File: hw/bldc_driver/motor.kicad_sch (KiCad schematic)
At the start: 103 parts, among them Q1 IRF540N, Q2 IRF540N, Q3 IRF540N, Q4 IRF540N, Q5 IRF540N, Q6 IRF540N, U10 TPS54202DDC, U11 AMC1200BDWV, U12 AMC1200BDWV, U13 AMC1200BDWV, U2 STGAP2SCM, U3 STGAP2SCM, U4 STGAP2SCM, U5 STGAP2SCM, U6 STGAP2SCM, U7 STGAP2SCM, U9 AMC1200BDWV

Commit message: feat: add CNCs
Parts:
- renumbered Rshunt to Rshunt1
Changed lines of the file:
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@@
 (kicad_sch
-	(version 20231120)
+	(version 20250114)
 	(generator "eeschema")
-	(generator_version "8.0")
+	(generator_version "9.0")
 	(paper "A4")
+	(rectangle
+		(start 124.46 13.335)
+		(end 147.955 165.1)
+		(stroke
+			(width -0.0001)
+			(type default)
+		)
+		(fill
+			(type color)
+			(color 0 132 0 0.3)
+		)
+	)
+	(rectangle
+		(start 139.7 13.335)
+		(end 167.64 94.615)
+		(stroke
+			(width -0.0001)
+			(type default)
+		)
+		(fill
+			(type color)
+			(color 0 132 0 0.3)
+		)
+	)
+	(rectangle
+		(start 167.64 13.335)
+		(end 254 94.615)
+		(stroke
+			(width -0.0001)
+			(type default)
+		)
+		(fill
+			(type color)
+			(color 132 0 0 0.3)
+		)
+	)
+	(rectangle
+		(start 147.955 94.615)
+		(end 254 165.1)
+		(stroke
+			(width -0.0001)
+			(type default)
+		)
+		(fill
+			(type color)
+			(color 132 0 0 0.3)
+		)
+	)
+	(rectangle
+		(start 155.575 119.38)
+		(end 246.38 161.29)
+		(stroke
+			(width 0)
+			(type default)
+		)
+		(fill
+			(type none)
+		)
+	)
+	(rectangle
+		(start 39.37 13.335)
+		(end 124.46 165.1)
+		(stroke
+			(width -0.0001)
+			(type default)
+		)
+		(fill
+			(type color)
+			(color 132 0 0 0.3)
+		)
+	)
+	(rectangle
+		(start 254 94.615)
+		(end 283.845 165.1)
+		(stroke
+			(width -0.0001)
+			(type default)
+		)
+		(fill
+			(type color)
+			(color 0 132 0 0.3)
+		)
+	)
+	(rectangle
+		(start 12.7 13.335)
+		(end 39.37 165.1)
+		(stroke
+			(width -0.0001)
+			(type default)
+		)
+		(fill
+			(type color)
+			(color 0 132 0 0.3)
+		)
+	)
+	(rectangle
+		(start 254 13.335)
+		(end 283.845 94.615)
+		(stroke
+			(width -0.0001)
+			(type default)
+		)
+		(fill
+			(type color)
+			(color 0 132 0 0.3)
+		)
+	)
+	(text "12V POWER"
+		(exclude_from_sim no)
+		(at 103.886 18.288 0)
+		(effects
+			(font
+				(size 3.81 3.81)
+				(color 255 0 0 1)
+			)
+		)
+	)
+	(text "3.3V MCU"
+		(exclude_from_sim no)
+		(at 269.494 17.272 0)
+		(effects
+			(font
+				(size 3.81 3.81)
+				(color 0 255 0 1)
+			)
+		)
+	)
+	(text "5V ADC DCDC"
+		(exclude_from_sim no)
+		(at 176.276 116.84 0)
+		(effects
+			(font
+				(size 3.81 3.81)
+				(color 255 0 0 1)
+			)
+		)
+	)
+	(text_box "Phase W Isolated Gate Drivers"
+		(exclude_from_sim no)
+		(at 157.48 13.335 0)
+		(size 31.75 7.62)
+		(margins 0.9525 0.9525 0.9525 0.9525)
+		(stroke
+			(width 0)
+			(type default)
+		)
+		(fill
+			(type none)
+		)
+		(effects
+			(font
+				(size 1.27 1.27)
+			)
+			(justify left top)
+		)
+	)
+	(text_box "Phase V Isolated Gate Drivers"
+		(exclude_from_sim no)
+		(at 36.195 89.535 0)
+		(size 31.75 7.62)
+		(margins 0.9525 0.9525 0.9525 0.9525)
+		(stroke
+			(width 0)
+			(type default)
+		)
+		(fill
+			(type none)
+		)
+		(effects
+			(font
+				(size 1.27 1.27)
+			)
+			(justify left top)
+		)
+	)
+	(text_box "Phase U Isolated Gate Drivers"
+		(exclude_from_sim no)
+		(at 36.83 13.335 0)
+		(size 31.75 7.62)
+		(margins 0.9525 0.9525 0.9525 0.9525)
+		(stroke
+			(width 0)
+			(type default)
+		)
+		(fill
+			(type none)
+		)
+		(effects
+			(font
+				(size 1.27 1.27)
+			)
+			(justify left top)
+		)
+	)
+	(text_box "Vout = Vref * (R4/R5 + 1) = 0.596 * (200k/27k + 1) = 5.010V"
+		(exclude_from_sim no)
+		(at 210.185 151.13 0)
+		(size 34.925 8.255)
+		(margins 0.9525 0.9525 0.9525 0.9525)
+		(stroke
+			(width 0)
+			(type default)
+		)
+		(fill
+			(type none)
+		)
+		(effects
+			(font
+				(size 1.27 1.27)
+			)
+			(justify left top)
+		)
+	)
 	(junction
 		(at 76.2 142.24)
@@
 		)
 	)
-	(rectangle
-		(start 124.46 13.335)
-		(end 147.955 165.1)
-		(stroke
-			(width -0.0001)
-			(type default)
-		)
-		(fill
-			(type color)
-			(color 0 132 0 0.3)
-		)
-	)
-	(rectangle
-		(start 139.7 13.335)
-		(end 167.64 94.615)
-		(stroke
-			(width -0.0001)
-			(type default)
-		)
-		(fill
-			(type color)
-			(color 0 132 0 0.3)
-		)
-	)
-	(rectangle
-		(start 167.64 13.335)
-		(end 254 94.615)
-		(stroke
-			(width -0.0001)
-			(type default)
-		)
-		(fill
-			(type color)
-			(color 132 0 0 0.3)
-		)
-	)
-	(rectangle
-		(start 147.955 94.615)
-		(end 254 165.1)
-		(stroke
-			(width -0.0001)
-			(type default)
-		)
-		(fill
-			(type color)
-			(color 132 0 0 0.3)
-		)
-	)
-	(rectangle
-		(start 155.575 119.38)
-		(end 246.38 161.29)
-		(stroke
-			(width 0)
-			(type default)
-		)
-		(fill
-			(type none)
-		)
-	)
-	(rectangle
-		(start 39.37 13.335)
-		(end 124.46 165.1)
-		(stroke
-			(width -0.0001)
-			(type default)
-		)
-		(fill
-			(type color)
-			(color 132 0 0 0.3)
-		)
-	)
-	(rectangle
-		(start 254 94.615)
-		(end 283.845 165.1)
-		(stroke
-			(width -0.0001)
-			(type default)
-		)
-		(fill
-			(type color)
-			(color 0 132 0 0.3)
-		)
-	)
-	(rectangle
-		(start 12.7 13.335)
-		(end 39.37 165.1)
-		(stroke
-			(width -0.0001)
-			(type default)
-		)
-		(fill
-			(type color)
-			(color 0 132 0 0.3)
-		)
-	)
-	(rectangle
-		(start 254 13.335)
-		(end 283.845 94.615)
-		(stroke
-			(width -0.0001)
-			(type default)
-		)
-		(fill
-			(type color)
-			(color 0 132 0 0.3)
-		)
-	)
-	(text_box "Phase W Isolated Gate Drivers"
-		(exclude_from_sim no)
-		(at 157.48 13.335 0)
-		(size 31.75 7.62)
-		(stroke
-			(width 0)
-			(type default)
-		)
-		(fill
-			(type none)
-		)
-		(effects
-			(font
-				(size 1.27 1.27)
-			)
-			(justify left top)
-		)
-	)
-	(text_box "Phase V Isolated Gate Drivers"
-		(exclude_from_sim no)
-		(at 36.195 89.535 0)
-		(size 31.75 7.62)
-		(stroke
-			(width 0)
-			(type default)
-		)
-		(fill
-			(type none)
-		)
-		(effects
-			(font
-				(size 1.27 1.27)
-			)
-			(justify left top)
-		)
-	)
-	(text_box "Phase U Isolated Gate Drivers"
-		(exclude_from_sim no)
-		(at 36.83 13.335 0)
-		(size 31.75 7.62)
-		(stroke
-			(width 0)
-			(type default)
-		)
-		(fill
-			(type none)
-		)
-		(effects
-			(font
-				(size 1.27 1.27)
-			)
-			(justify left top)
-		)
-	)
-	(text_box "Vout = Vref * (R4/R5 + 1) = 0.596 * (200k/27k + 1) = 5.010V"
-		(exclude_from_sim no)
-		(at 210.185 151.13 0)
-		(size 34.925 8.255)
-		(stroke
-			(width 0)
-			(type default)
-		)
-		(fill
-			(type none)
-		)
-		(effects
-			(font
-				(size 1.27 1.27)
-			)
-			(justify left top)
-		)
-	)
-	(text "12V POWER"
-		(exclude_from_sim no)
-		(at 103.886 18.288 0)
-		(effects
-			(font
-				(size 3.81 3.81)
-				(color 255 0 0 1)
-			)
-		)
-	)
-	(text "3.3V MCU"
-		(exclude_from_sim no)
-		(at 269.494 17.272 0)
-		(effects
-			(font
-				(size 3.81 3.81)
-				(color 0 255 0 1)
-			)
-		)
-	)
-	(text "5V ADC DCDC"
-		(exclude_from_sim no)
-		(at 176.276 116.84 0)
-		(effects
-			(font
-				(size 3.81 3.81)
-				(color 255 0 0 1)
-			)
-		)
-	)
 	(hierarchical_label "PH_U_HI"
 		(shape input)
@@
 		(on_board yes)
 		(dnp no)
-		(property "Reference" "Rshunt"
+		(property "Reference" "Rshunt1"
 			(at 227.584 108.712 90)
 			(effects
@@
 			(project ""
 				(path "/6f0070f8-99b2-4a48-98f9-774d985c191f/19ba0eb6-9d44-4933-bb79-a8302d3dae46"
-					(reference "Rshunt")
+					(reference "Rshunt1")
 					(unit 1)
 				)

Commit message: feat: start PCB
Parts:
- C10, C12, C14, C33, C35, C37, C43, C45, C47, C49, C51, C53: footprint 0805 (2012 Metric) -> Capacitor_SMD:C_0805_2012Metric_Pad1.18x1.45mm_HandSolder
- Rshunt1: value R -> HoLLR2512-3W-15mR-1%
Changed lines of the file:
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@@
 			)
 		)
-		(property "Footprint" "0805 (2012 Metric)"
+		(property "Footprint" "Capacitor_SMD:C_0805_2012Metric_Pad1.18x1.45mm_HandSolder"
 			(at 45.4152 138.43 0)
 			(effects
@@
 			)
 		)
-		(property "Footprint" "0805 (2012 Metric)"
+		(property "Footprint" "Capacitor_SMD:C_0805_2012Metric_Pad1.18x1.45mm_HandSolder"
 			(at 152.0952 30.48 0)
 			(effects
@@
 			)
 		)
-		(property "Footprint" "0805 (2012 Metric)"
+		(property "Footprint" "Capacitor_SMD:C_0805_2012Metric_Pad1.18x1.45mm_HandSolder"
 			(at 30.1752 138.43 0)
 			(effects
@@
 			)
 		)
-		(property "Footprint" "0805 (2012 Metric)"
+		(property "Footprint" "Capacitor_SMD:C_0805_2012Metric_Pad1.18x1.45mm_HandSolder"
 			(at 174.9552 29.21 0)
 			(effects
@@
 			)
 		)
-		(property "Footprint" "0805 (2012 Metric)"
+		(property "Footprint" "Capacitor_SMD:C_0805_2012Metric_Pad1.18x1.45mm_HandSolder"
 			(at 25.0952 106.68 0)
 			(effects
@@
 			)
 		)
-		(property "Value" "R"
-			(at 229.87 106.172 90)
+		(property "Value" "HoLLR2512-3W-15mR-1%"
+			(at 225.552 118.618 90)
 			(effects
 				(font
@@
 			)
 		)
-		(property "Footprint" "0805 (2012 Metric)"
+		(property "Footprint" "Capacitor_SMD:C_0805_2012Metric_Pad1.18x1.45mm_HandSolder"
 			(at 45.4152 62.23 0)
 			(effects
@@
 			)
 		)
-		(property "Footprint" "0805 (2012 Metric)"
+		(property "Footprint" "Capacitor_SMD:C_0805_2012Metric_Pad1.18x1.45mm_HandSolder"
 			(at 46.6852 30.48 0)
 			(effects
@@
 			)
 		)
-		(property "Footprint" "0805 (2012 Metric)"
+		(property "Footprint" "Capacitor_SMD:C_0805_2012Metric_Pad1.18x1.45mm_HandSolder"
 			(at 46.6852 105.41 0)
 			(effects
@@
 			)
 		)
-		(property "Footprint" "0805 (2012 Metric)"
+		(property "Footprint" "Capacitor_SMD:C_0805_2012Metric_Pad1.18x1.45mm_HandSolder"
 			(at 173.6852 68.58 0)
 			(effects
@@
 			)
 		)
-		(property "Footprint" "0805 (2012 Metric)"
+		(property "Footprint" "Capacitor_SMD:C_0805_2012Metric_Pad1.18x1.45mm_HandSolder"
 			(at 30.1752 62.23 0)
 			(effects
@@
 			)
 		)
-		(property "Footprint" "0805 (2012 Metric)"
+		(property "Footprint" "Capacitor_SMD:C_0805_2012Metric_Pad1.18x1.45mm_HandSolder"
 			(at 25.0952 30.48 0)
 			(effects
@@
 			)
 		)
-		(property "Footprint" "0805 (2012 Metric)"
+		(property "Footprint" "Capacitor_SMD:C_0805_2012Metric_Pad1.18x1.45mm_HandSolder"
 			(at 158.4452 68.58 0)
 			(effects

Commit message: bldc: start placement
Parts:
- removed Q1: IRF540N, Package_TO_SOT_THT:TO-220-3_Horizontal_TabDown, symbol Transistor_FET:IRF540N
- removed TP4: TestPoint_Flag, TestPoint:TestPoint_Plated_Hole_D2.0mm, symbol Connector:TestPoint_Flag
- added Q7: IRF540N, Package_TO_SOT_THT:TO-220-3_Horizontal_TabDown, symbol Transistor_FET:IRF540N
- Rshunt1: footprint (none) -> Resistor_SMD:R_2512_6332Metric_Pad1.40x3.35mm_HandSolder
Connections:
- net MOTOR_U: now also Q7.2 (D)
- net at R26.2, R27.2, U3.7 (CLAMP): now also Q7.1 (G)
- net at C23.1, D4.1 (A), D4.3 (A)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: now also Q7.3 (S)
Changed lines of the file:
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@@
 	)
 	(junction
-		(at 76.2 66.04)
-		(diameter 0)
-		(color 0 0 0 0)
-	)
-	(junction
 		(at 67.31 151.13)
 		(diameter 0)
@@
 	)
 	(junction
+		(at 76.2 66.04)
+		(diameter 0)
+		(color 0 0 0 0)
+	)
+	(junction
 		(at 34.29 130.81)
 		(diameter 0)
@@
 	(wire
 		(pts
-			(xy 175.26 123.19) (xy 175.26 132.08)
-		)
-		(stroke
-			(width 0)
-			(type default)
-		)
-	)
-	(wire
-		(pts
 			(xy 93.98 73.66) (xy 104.14 73.66)
 		)
@@
 	)
 	(symbol
-		(lib_id "Connector:TestPoint_Flag")
-		(at 175.26 123.19 0)
-		(unit 1)
-		(exclude_from_sim no)
-		(in_bom yes)
-		(on_board yes)
-		(dnp no)
-		(property "Reference" "TP4"
-			(at 182.88 120.5229 0)
-			(effects
-				(font
-					(size 1.27 1.27)
-				)
-				(justify left)
-			)
-		)
-		(property "Value" "TestPoint_Flag"
-			(at 176.022 118.364 0)
-			(effects
-				(font
-					(size 1.27 1.27)
-				)
-				(justify left)
-				(hide yes)
-			)
-		)
-		(property "Footprint" "TestPoint:TestPoint_Plated_Hole_D2.0mm"
-			(at 180.34 123.19 0)
-			(effects
-				(font
-					(size 1.27 1.27)
-				)
-				(hide yes)
-			)
-		)
-		(property "Datasheet" "~"
-			(at 180.34 123.19 0)
-			(effects
-				(font
-					(size 1.27 1.27)
-				)
-				(hide yes)
-			)
-		)
-		(property "Description" "test point (alternative flag-style design)"
-			(at 175.26 123.19 0)
-			(effects
-				(font
-					(size 1.27 1.27)
-				)
-				(hide yes)
-			)
-		)
-		(pin "1"
-		)
-		(instances
-			(project "bldc_driver"
-				(path "/6f0070f8-99b2-4a48-98f9-774d985c191f/19ba0eb6-9d44-4933-bb79-a8302d3dae46"
-					(reference "TP4")
-					(unit 1)
-				)
-			)
-		)
-	)
-	(symbol
 		(lib_id "power:+VDC")
 		(at 76.2 21.59 0)
@@
 	)
 	(symbol
-		(lib_id "Transistor_FET:IRF540N")
-		(at 73.66 71.12 0)
-		(unit 1)
-		(exclude_from_sim no)
-		(in_bom yes)
-		(on_board yes)
-		(dnp no)
-		(property "Reference" "Q1"
-			(at 76.962 67.818 0)
-			(effects
-				(font
-					(size 1.27 1.27)
-				)
-				(justify left)
-			)
-		)
-		(property "Value" "IRF540N"
-			(at 76.962 74.93 0)
-			(effects
-				(font
-					(size 1.27 1.27)
-				)
-				(justify left)
-			)
-		)
-		(property "Footprint" "Package_TO_SOT_THT:TO-220-3_Horizontal_TabDown"
-			(at 78.74 73.025 0)
-			(effects
-				(font
-					(size 1.27 1.27)
-					(italic yes)
-				)
-				(justify left)
-				(hide yes)
-			)
-		)
-		(property "Datasheet" "http://www.irf.com/product-info/datasheets/data/irf540n.pdf"
-			(at 78.74 74.93 0)
-			(effects
-				(font
-					(size 1.27 1.27)
-				)
-				(justify left)
-				(hide yes)
-			)
-		)
-		(property "Description" "33A Id, 100V Vds, HEXFET N-Channel MOSFET, TO-220"
-			(at 73.66 71.12 0)
-			(effects
-				(font
-					(size 1.27 1.27)
-				)
-				(hide yes)
-			)
-		)
-		(pin "2"
-		)
-		(pin "3"
-		)
-		(pin "1"
-		)
-		(instances
-			(project "bldc_driver"
-				(path "/6f0070f8-99b2-4a48-98f9-774d985c191f/19ba0eb6-9d44-4933-bb79-a8302d3dae46"
-					(reference "Q1")
-					(unit 1)
-				)
-			)
-		)
-	)
-	(symbol
 		(lib_id "Driver_FET:STGAP2SCM")
 		(at 167.64 41.91 0)
@@
 	)
 	(symbol
+		(lib_id "Transistor_FET:IRF540N")
+		(at 73.66 71.12 0)
+		(unit 1)
+		(exclude_from_sim no)
+		(in_bom yes)
+		(on_board yes)
+		(dnp no)
+		(property "Reference" "Q7"
+			(at 76.962 67.818 0)
+			(effects
+				(font
+					(size 1.27 1.27)
+				)
+				(justify left)
+			)
+		)
+		(property "Value" "IRF540N"
+			(at 76.962 74.93 0)
+			(effects
+				(font
+					(size 1.27 1.27)
+				)
+				(justify left)
+			)
+		)
+		(property "Footprint" "Package_TO_SOT_THT:TO-220-3_Horizontal_TabDown"
+			(at 78.74 73.025 0)
+			(effects
+				(font
+					(size 1.27 1.27)
+					(italic yes)
+				)
+				(justify left)
+				(hide yes)
+			)
+		)
+		(property "Datasheet" "http://www.irf.com/product-info/datasheets/data/irf540n.pdf"
+			(at 78.74 74.93 0)
+			(effects
+				(font
+					(size 1.27 1.27)
+				)
+				(justify left)
+				(hide yes)
+			)
+		)
+		(property "Description" "33A Id, 100V Vds, HEXFET N-Channel MOSFET, TO-220"
+			(at 73.66 71.12 0)
+			(effects
+				(font
+					(size 1.27 1.27)
+				)
+				(hide yes)
+			)
+		)
+		(pin "2"
+		)
+		(pin "3"
+		)
+		(pin "1"
+		)
+		(instances
+			(project "bldc_driver"
+				(path "/6f0070f8-99b2-4a48-98f9-774d985c191f/19ba0eb6-9d44-4933-bb79-a8302d3dae46"
+					(reference "Q7")
+					(unit 1)
+				)
+			)
+		)
+	)
+	(symbol
 		(lib_id "Driver_FET:STGAP2SCM")
 		(at 39.37 118.11 0)
@@
 			)
 		)
-		(property "Footprint" ""
+		(property "Footprint" "Resistor_SMD:R_2512_6332Metric_Pad1.40x3.35mm_HandSolder"
 			(at 228.092 105.41 90)
 			(effects

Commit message: bldc: placement mostly done
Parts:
- R7: footprint Resistor_SMD:R_0201_0603Metric_Pad0.64x0.40mm_HandSolder -> Resistor_SMD:R_0603_1608Metric_Pad0.98x0.95mm_HandSolder
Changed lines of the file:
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@@
 			)
 		)
-		(property "Footprint" "Resistor_SMD:R_0201_0603Metric_Pad0.64x0.40mm_HandSolder"
+		(property "Footprint" "Resistor_SMD:R_0603_1608Metric_Pad0.98x0.95mm_HandSolder"
 			(at 173.482 137.16 90)
 			(effects

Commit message: full route
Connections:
- net GND: no longer C33.2, C34.2, C35.2, C36.2, C37.2, C38.2, C45.2, C46.2, C49.2, C50.2, C53.2, C54.2
- net GNDPWR: now also C33.2, C34.2, C35.2, C36.2, C37.2, C38.2, C45.2, C46.2, C49.2, C50.2, C53.2, C54.2

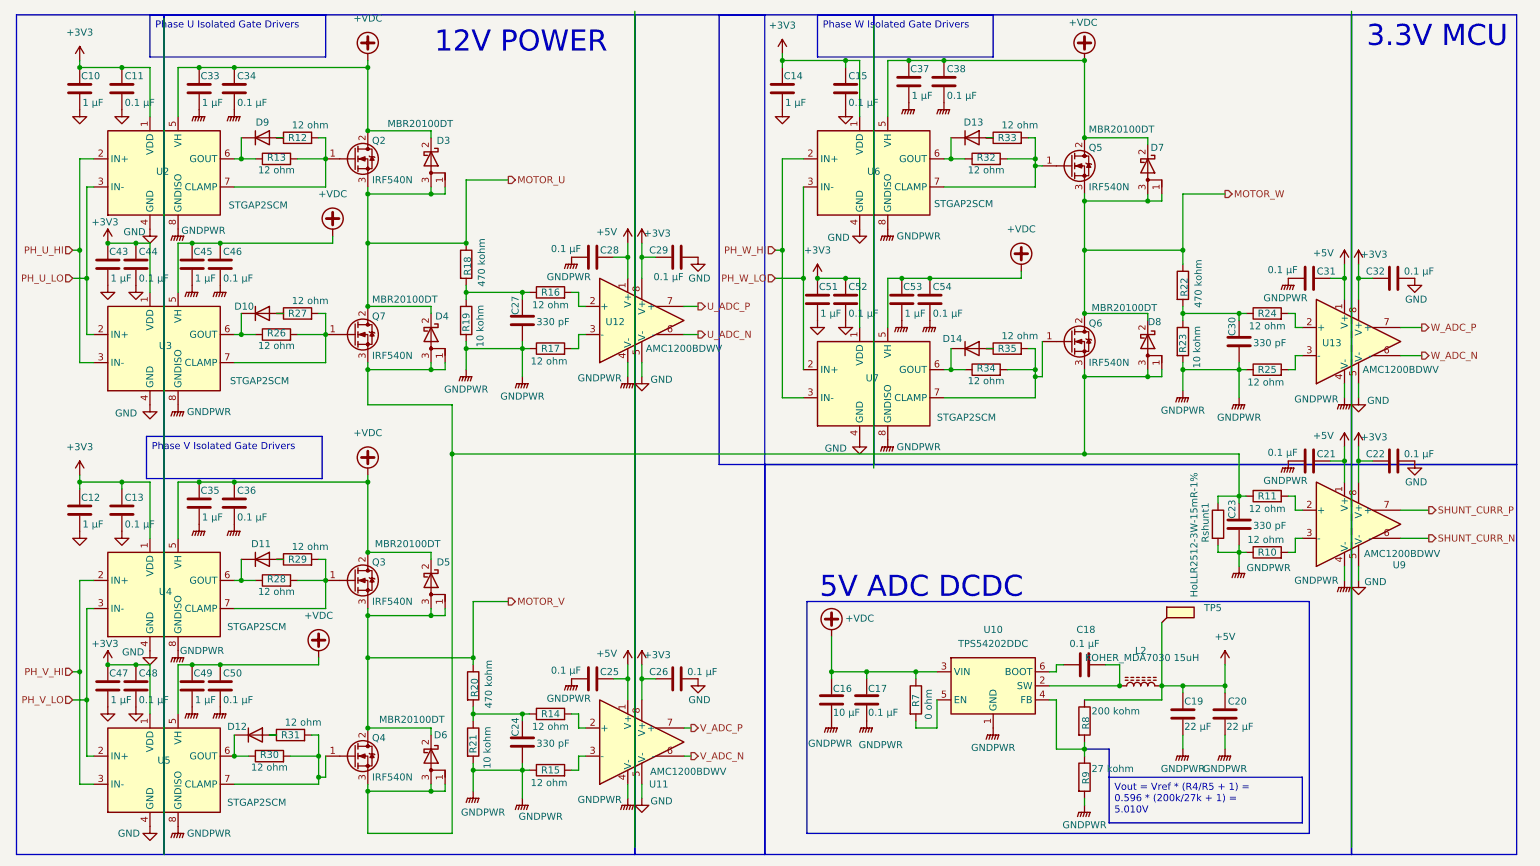
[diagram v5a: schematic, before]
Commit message: fmu: update power supply and other connections
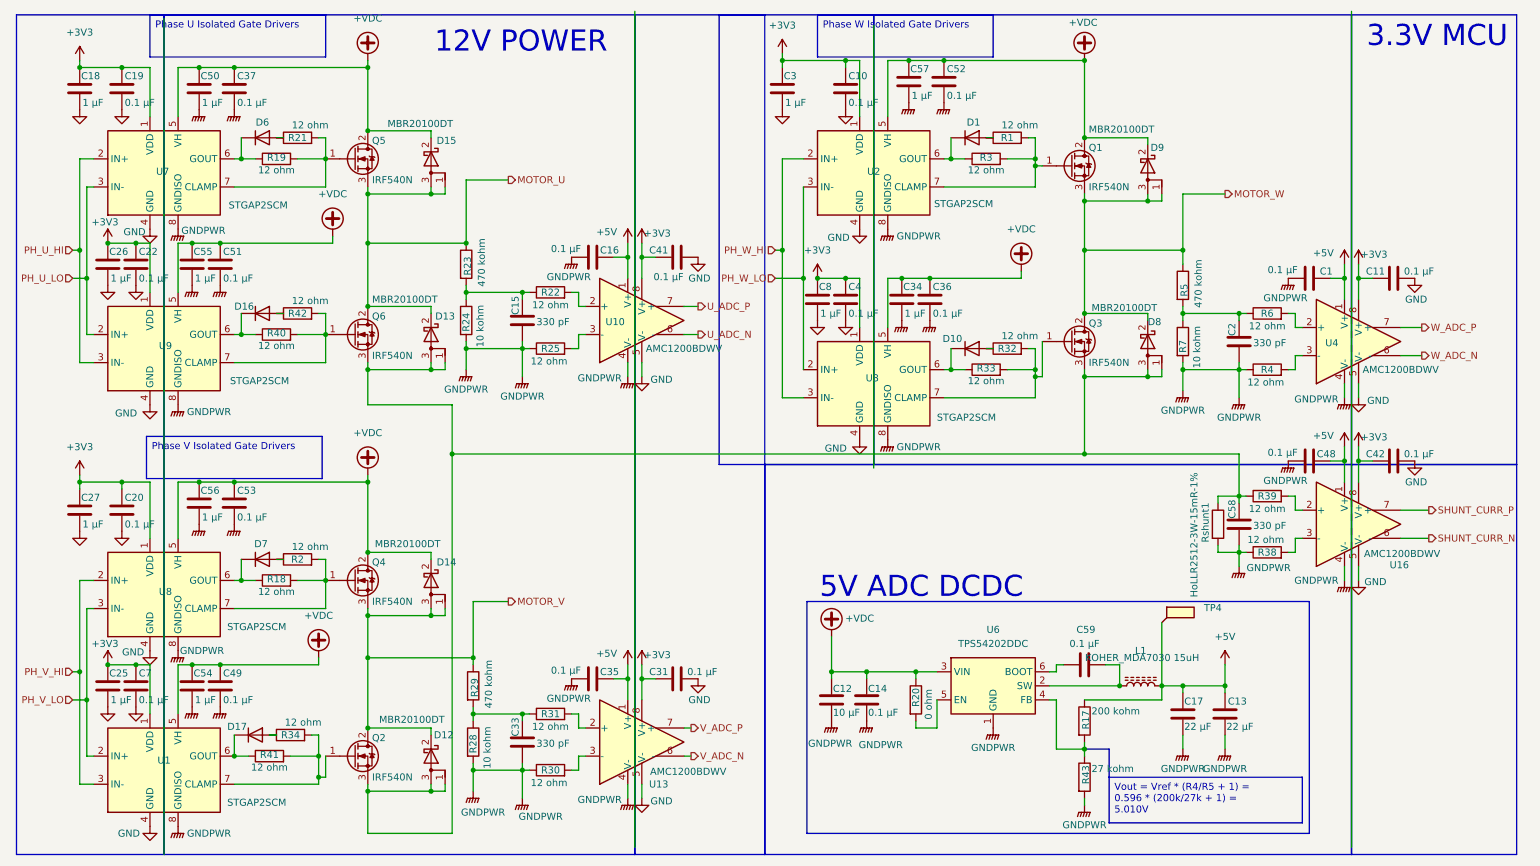
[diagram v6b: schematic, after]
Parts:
- renumbered C31 to C1, C15 to C10, C32 to C11, C16 to C12, C20 to C13, C17 to C14, C27 to C15, C28 to C16, C19 to C17, C10 to C18, C11 to C19, C30 to C2, C13 to C20, C44 to C22, C47 to C25, C43 to C26, C12 to C27, C14 to C3, C26 to C31, C24 to C33, C53 to C34, C25 to C35, C54 to C36, C34 to C37, C52 to C4, C29 to C41, C22 to C42, C21 to C48, C50 to C49, C33 to C50, C46 to C51, C38 to C52, C36 to C53, C49 to C54, C45 to C55, C35 to C56, C37 to C57, C23 to C58, C18 to C59, C48 to C7, C51 to C8, D13 to D1, D14 to D10, D6 to D12, D4 to D13, D5 to D14, D3 to D15, D10 to D16, D12 to D17, D9 to D6, D11 to D7, D7 to D9, L2 to L1, Q5 to Q1, Q4 to Q2, Q6 to Q3, Q3 to Q4, Q2 to Q5, Q7 to Q6, R33 to R1, R8 to R17, R28 to R18, R13 to R19, R29 to R2, R7 to R20, R12 to R21, R16 to R22, R18 to R23, R19 to R24, R17 to R25, R21 to R28, R20 to R29, R32 to R3, R15 to R30, R14 to R31, R35 to R32, R34 to R33, R31 to R34, R10 to R38, R11 to R39, R25 to R4, R26 to R40, R30 to R41, R27 to R42, R9 to R43, R22 to R5, R24 to R6, R23 to R7, TP5 to TP4, U5 to U1, U12 to U10, U11 to U13, U9 to U16, U6 to U2, U7 to U3, U13 to U4, U10 to U6, U2 to U7, U4 to U8, U3 to U9
